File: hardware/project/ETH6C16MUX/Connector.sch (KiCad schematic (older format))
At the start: 2 parts, among them J801 C64AC, J802 Conn_01x06

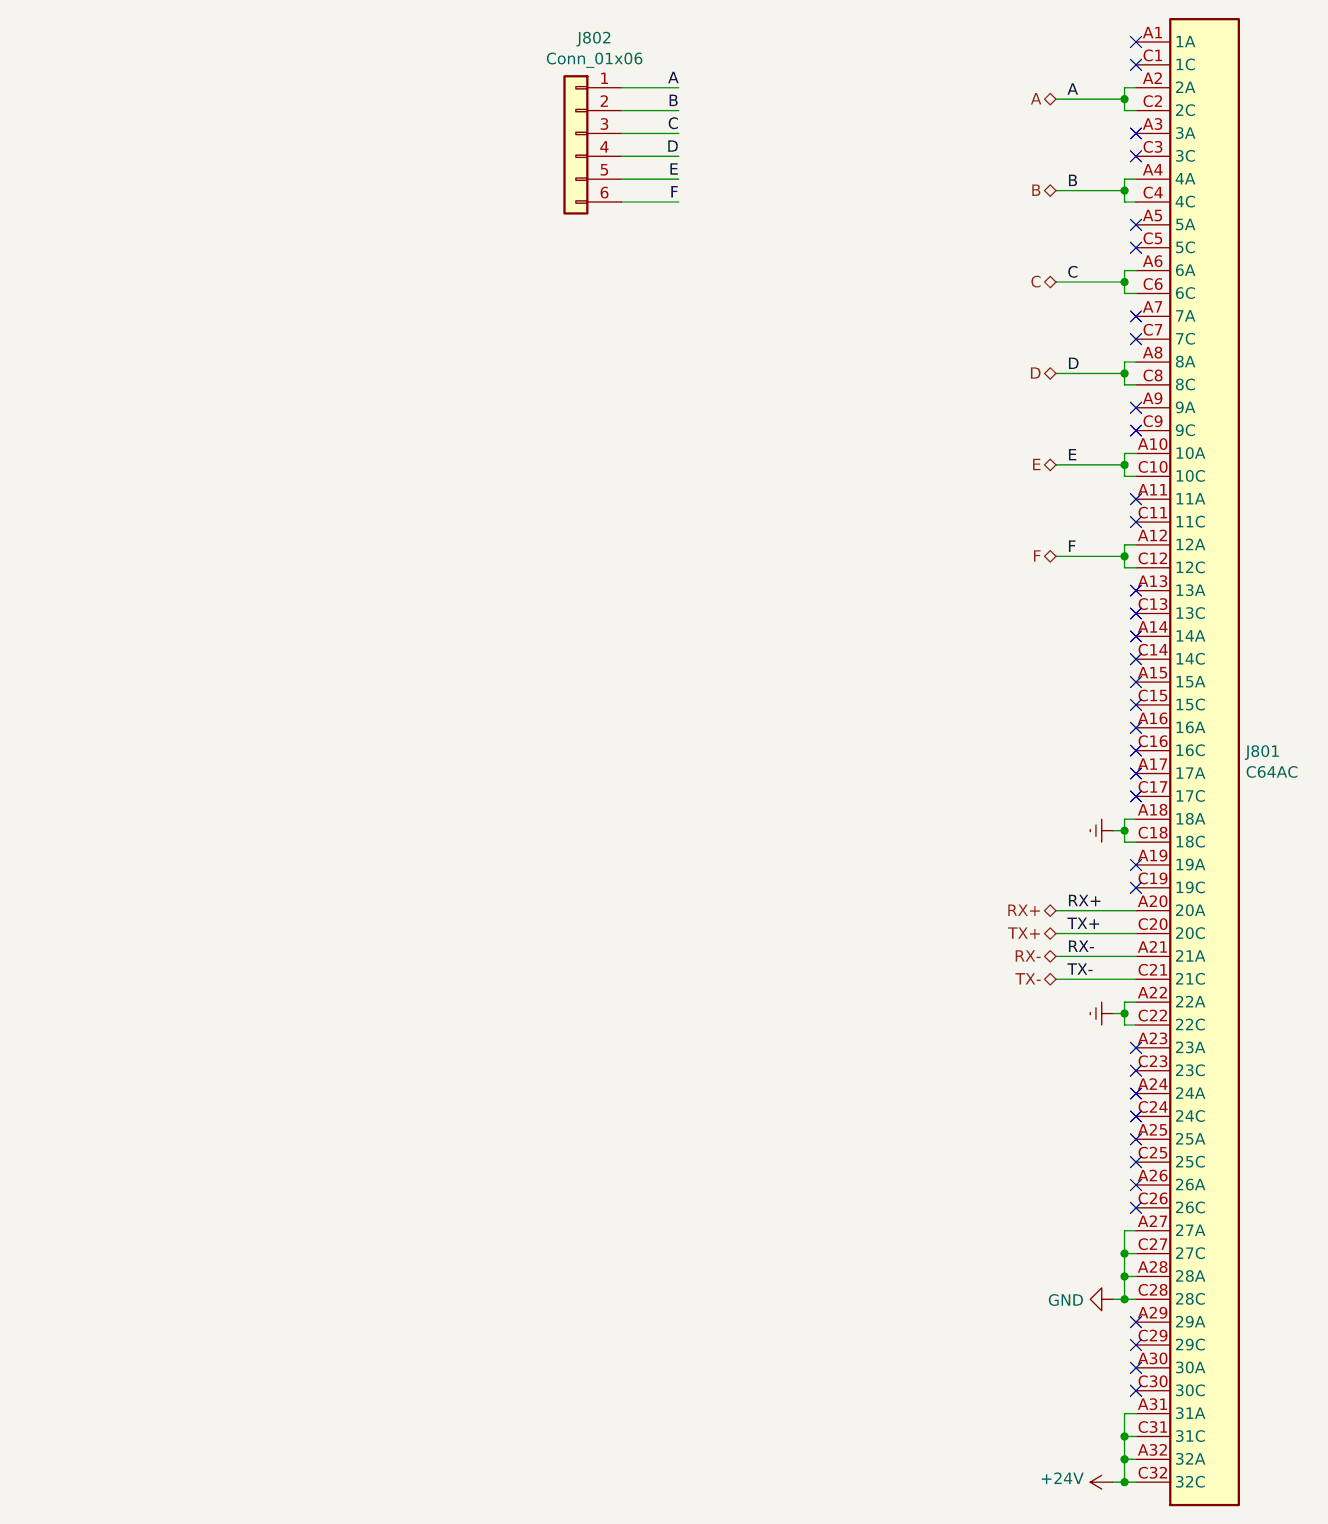
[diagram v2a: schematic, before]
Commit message: PCB layout, board to board connector changed.
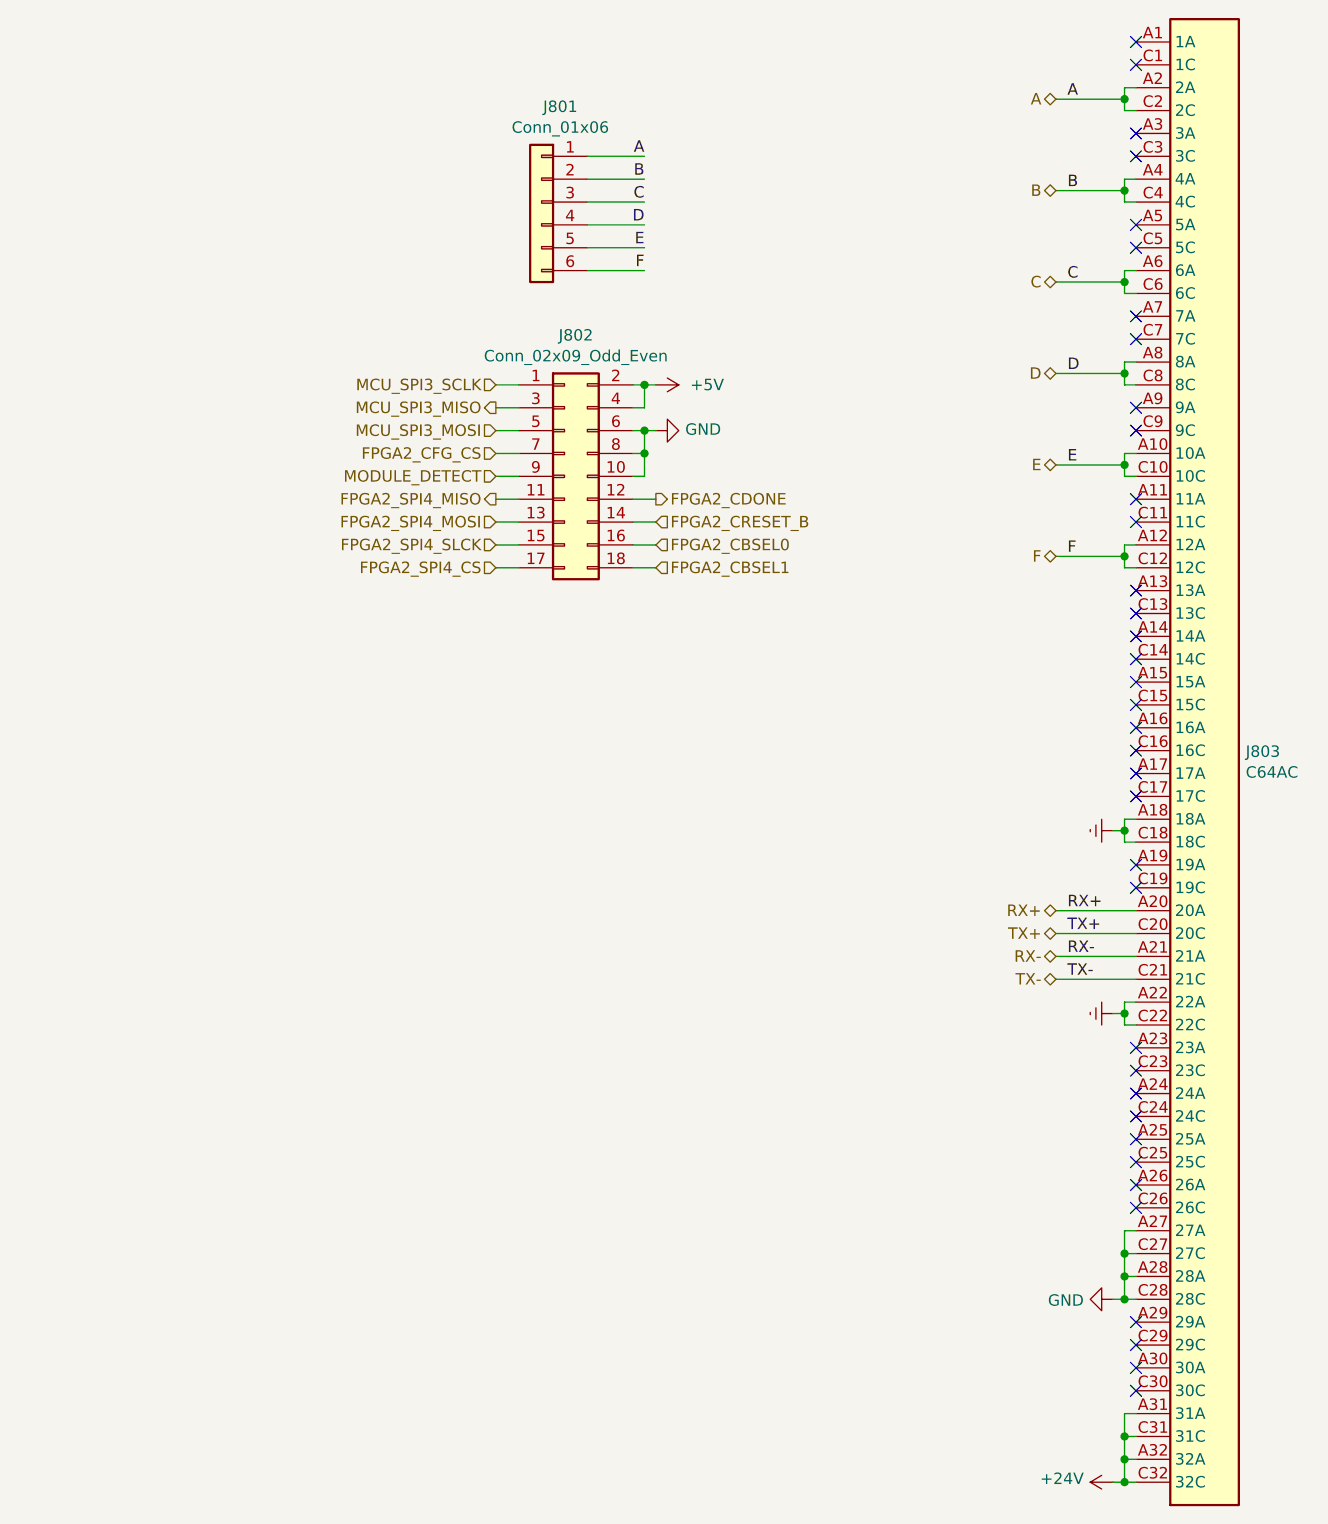
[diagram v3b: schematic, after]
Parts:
- removed J802: Conn_01x06, symbol Connector_Generic:Conn_01x06
- added J801: Conn_01x06, Connector_PinSocket_2.54mm:PinSocket_1x06_P2.54mm_Vertical, symbol Connector_Generic:Conn_01x06
- added J802: Conn_02x09_Odd_Even, Connector_PinSocket_2.54mm:PinSocket_2x09_P2.54mm_Vertical, symbol Connector_Generic:Conn_02x09_Odd_Even
- renumbered J801 to J803
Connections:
- net A: now also J801.1 (Pin_1)
- net B: now also J801.2 (Pin_2)
- net C: now also J801.3 (Pin_3)
- net D: now also J801.4 (Pin_4)
- net E: now also J801.5 (Pin_5)
- net F: now also J801.6 (Pin_6)
- net GND: now also J802.10 (Pin_10), J802.6 (Pin_6), J802.8 (Pin_8)
- new net +5V: J802.2 (Pin_2), J802.4 (Pin_4)
- new net FPGA2_CBSEL0: J802.16 (Pin_16)
- new net FPGA2_CBSEL1: J802.18 (Pin_18)
- new net FPGA2_CDONE: J802.12 (Pin_12)
- new net FPGA2_CFG_CS: J802.7 (Pin_7)
- new net FPGA2_CRESET_B: J802.14 (Pin_14)
- new net FPGA2_SPI4_CS: J802.17 (Pin_17)
- new net FPGA2_SPI4_MISO: J802.11 (Pin_11)
- new net FPGA2_SPI4_MOSI: J802.13 (Pin_13)
- new net FPGA2_SPI4_SLCK: J802.15 (Pin_15)
- new net MCU_SPI3_MISO: J802.3 (Pin_3)
- new net MCU_SPI3_MOSI: J802.5 (Pin_5)
- new net MCU_SPI3_SCLK: J802.1 (Pin_1)
- new net MODULE_DETECT: J802.9 (Pin_9)
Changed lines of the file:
@@
 $Descr A4 11693 8268
 encoding utf-8
-Sheet 8 9
+Sheet 8 8
 Title ""
 Date ""
@@
 $EndDescr
 $Comp
-L Connector:C64AC J801
+L Connector:C64AC J803
 U 1 1 5DB3A84B
 P 5950 4000
-F 0 "J801" H 6130 4096 50  0000 L CNN
+F 0 "J803" H 6130 4096 50  0000 L CNN
 F 1 "C64AC" H 6130 4005 50  0000 L CNN
 F 2 "ETH6C16MXU:Socket_DIN41612-CaseC1-AC-Male-64Pin-2rows" H 5950 4050 50  0001 C CNN
@@
 	5600 6200 5600 6100
 $Comp
-L power:+24V #PWR0805
+L power:+24V #PWR0808
 U 1 1 5D7D1F7C
 P 5550 7100
-F 0 "#PWR0805" H 5550 6950 50  0001 C CNN
+F 0 "#PWR0808" H 5550 6950 50  0001 C CNN
 F 1 "+24V" V 5565 7228 50  0000 L CNN
 F 2 "" H 5550 7100 50  0001 C CNN
@@
 Connection ~ 5600 7100
 $Comp
-L power:GND #PWR0804
+L power:GND #PWR0807
 U 1 1 5D7D46BE
 P 5550 6300
-F 0 "#PWR0804" H 5550 6050 50  0001 C CNN
+F 0 "#PWR0807" H 5550 6050 50  0001 C CNN
 F 1 "GND" V 5555 6172 50  0000 R CNN
 F 2 "" H 5550 6300 50  0001 C CNN
@@
 RX-
 $Comp
-L power:Earth #PWR0803
+L power:Earth #PWR0806
 U 1 1 5D7F1666
 P 5550 5050
-F 0 "#PWR0803" H 5550 4800 50  0001 C CNN
+F 0 "#PWR0806" H 5550 4800 50  0001 C CNN
 F 1 "Earth" H 5550 4900 50  0001 C CNN
 F 2 "" H 5550 5050 50  0001 C CNN
@@
 	5600 5050 5600 5000
 $Comp
-L power:Earth #PWR0802
+L power:Earth #PWR0805
 U 1 1 5D7F6C0C
 P 5550 4250
-F 0 "#PWR0802" H 5550 4000 50  0001 C CNN
+F 0 "#PWR0805" H 5550 4000 50  0001 C CNN
 F 1 "Earth" H 5550 4100 50  0001 C CNN
 F 2 "" H 5550 4250 50  0001 C CNN
@@
 Text Label 5350 3050 0    50   ~ 0
 F
-Text Label 3650 1000 2    50   ~ 0
+Wire Wire Line
+	3550 2500 3500 2500
+Wire Wire Line
+	3450 2600 3500 2600
+Wire Wire Line
+	3500 2500 3500 2600
+Connection ~ 3500 2500
+Wire Wire Line
+	3450 2500 3500 2500
+Wire Wire Line
+	3500 2300 3550 2300
+Wire Wire Line
+	3500 2300 3450 2300
+Connection ~ 3500 2300
+Wire Wire Line
+	3500 2400 3500 2300
+Wire Wire Line
+	3450 2400 3500 2400
+Wire Wire Line
+	2850 2700 2950 2700
+Wire Wire Line
+	2850 2900 2950 2900
+Wire Wire Line
+	2950 2800 2850 2800
+Wire Wire Line
+	2850 3100 2950 3100
+Wire Wire Line
+	2950 3000 2850 3000
+Wire Wire Line
+	2850 2600 2950 2600
+Wire Wire Line
+	3450 3100 3550 3100
+Wire Wire Line
+	3550 3000 3450 3000
+Wire Wire Line
+	3550 2900 3450 2900
+Wire Wire Line
+	3550 2800 3450 2800
+Wire Wire Line
+	2950 2500 2850 2500
+Wire Wire Line
+	2850 2400 2950 2400
+Wire Wire Line
+	2950 2300 2850 2300
+Text HLabel 2850 2700 0    50   Input ~ 0
+MODULE_DETECT
+$Comp
+L power:GND #PWR0804
+U 1 1 5D777B58
+P 3550 2500
+AR Path="/5DB25E5A/5D777B58" Ref="#PWR0804"  Part="1"
+AR Path="/5D7599BA/5D777B58" Ref="#PWR?"  Part="1"
+F 0 "#PWR0804" H 3550 2250 50  0001 C CNN
+F 1 "GND" V 3555 2372 50  0000 R CNN
+F 2 "" H 3550 2500 50  0001 C CNN
+F 3 "" H 3550 2500 50  0001 C CNN
+	1    3550 2500
+	0    -1   -1   0
+$EndComp
+$Comp
+L power:+5V #PWR0803
+U 1 1 5D777B5E
+P 3550 2300
+AR Path="/5DB25E5A/5D777B5E" Ref="#PWR0803"  Part="1"
+AR Path="/5D7599BA/5D777B5E" Ref="#PWR?"  Part="1"
+F 0 "#PWR0803" H 3550 2150 50  0001 C CNN
+F 1 "+5V" V 3550 2450 50  0000 L CNN
+F 2 "" H 3550 2300 50  0001 C CNN
+F 3 "" H 3550 2300 50  0001 C CNN
+	1    3550 2300
+	0    1    1    0
+$EndComp
+Text HLabel 2850 2300 0    50   Input ~ 0
+MCU_SPI3_SCLK
+Text HLabel 2850 2400 0    50   Output ~ 0
+MCU_SPI3_MISO
+Text HLabel 2850 2500 0    50   Input ~ 0
+MCU_SPI3_MOSI
+Text HLabel 3550 3000 2    50   Input ~ 0
+FPGA2_CBSEL0
+Text HLabel 3550 3100 2    50   Input ~ 0
+FPGA2_CBSEL1
+Text HLabel 3550 2900 2    50   Input ~ 0
+FPGA2_CRESET_B
+Text HLabel 3550 2800 2    50   Output ~ 0
+FPGA2_CDONE
+Text HLabel 2850 3000 0    50   Input ~ 0
+FPGA2_SPI4_SLCK
+Text HLabel 2850 3100 0    50   Input ~ 0
+FPGA2_SPI4_CS
+Text HLabel 2850 2800 0    50   Output ~ 0
+FPGA2_SPI4_MISO
+Text HLabel 2850 2900 0    50   Input ~ 0
+FPGA2_SPI4_MOSI
+Text HLabel 2850 2600 0    50   Input ~ 0
+FPGA2_CFG_CS
+Text Label 3500 1300 2    50   ~ 0
 A
-Text Label 3650 1100 2    50   ~ 0
+Text Label 3500 1400 2    50   ~ 0
 B
-Text Label 3650 1200 2    50   ~ 0
+Text Label 3500 1500 2    50   ~ 0
 C
-Text Label 3650 1300 2    50   ~ 0
+Text Label 3500 1600 2    50   ~ 0
 D
-Text Label 3650 1400 2    50   ~ 0
+Text Label 3500 1700 2    50   ~ 0
 E
-Text Label 3650 1500 2    50   ~ 0
+Text Label 3500 1800 2    50   ~ 0
 F
 $Comp
-L Connector_Generic:Conn_01x06 J802
-U 1 1 61D03557
-P 3200 1200
-F 0 "J802" H 3118 1617 50  0000 C CNN
-F 1 "Conn_01x06" H 3118 1526 50  0000 C CNN
-F 2 "" H 3200 1200 50  0001 C CNN
-F 3 "~" H 3200 1200 50  0001 C CNN
-	1    3200 1200
+L Connector_Generic:Conn_01x06 J?
+U 1 1 5D777B7C
+P 3050 1500
+AR Path="/5D7599BA/5D777B7C" Ref="J?"  Part="1"
+AR Path="/5DB25E5A/5D777B7C" Ref="J801"  Part="1"
+F 0 "J801" H 2968 1917 50  0000 C CNN
+F 1 "Conn_01x06" H 2968 1826 50  0000 C CNN
+F 2 "Connector_PinSocket_2.54mm:PinSocket_1x06_P2.54mm_Vertical" H 3050 1500 50  0001 C CNN
+F 3 "~" H 3050 1500 50  0001 C CNN
+	1    3050 1500
 	-1   0    0    -1
 $EndComp
 Wire Wire Line
-	3400 1000 3650 1000
-Wire Wire Line
-	3400 1100 3650 1100
-Wire Wire Line
-	3400 1200 3650 1200
-Wire Wire Line
-	3400 1300 3650 1300
-Wire Wire Line
-	3400 1400 3650 1400
-Wire Wire Line
-	3400 1500 3650 1500
+	3250 1300 3500 1300
+Wire Wire Line
+	3250 1400 3500 1400
+Wire Wire Line
+	3250 1500 3500 1500
+Wire Wire Line
+	3250 1600 3500 1600
+Wire Wire Line
+	3250 1700 3500 1700
+Wire Wire Line
+	3250 1800 3500 1800
+$Comp
+L Connector_Generic:Conn_02x09_Odd_Even J802
+U 1 1 5D8AE50E
+P 3150 2700
+F 0 "J802" H 3200 3317 50  0000 C CNN
+F 1 "Conn_02x09_Odd_Even" H 3200 3226 50  0000 C CNN
+F 2 "Connector_PinSocket_2.54mm:PinSocket_2x09_P2.54mm_Vertical" H 3150 2700 50  0001 C CNN
+F 3 "~" H 3150 2700 50  0001 C CNN
+	1    3150 2700
+	1    0    0    -1
+$EndComp
+Wire Wire Line
+	3500 2600 3500 2700
+Wire Wire Line
+	3500 2700 3450 2700
+Connection ~ 3500 2600
 $EndSCHEMATC
